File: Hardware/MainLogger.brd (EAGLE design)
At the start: 90 x 70 mm, 163 parts, among them J2 GEMS_POWER_PLUGINPUT, J3 CONN_TALON_LOGGER, J4 U.FL, J5 CONN_TALON_LOGGER, J6 CONN_TALON_LOGGER, J8 CONN_TALON_LOGGER, Q1 DMG3404, Q2 MOSFET_PCH-DMP3036SFG, Q3 MOSFET_PCH-DMP3036SFG, Q4 DMG3404, Q5 NX2301P, U1 MMC5633, U10 MXC6655, U11 FXMAR2102UMLP, U12 MCP79412SOIC, U13 SN74LVC1G17DCK, U14 TPL5010DDC, U15 MIC842L, U16 TPL5010DDC, U17 TPL5010DDC, U18 HALL_EFFECT_SI7201, U19 LP59073.3VYKE, U2 PAC1934QFN, U21 MIC22602, U3 LTC4412S6, U4 BQ25616, U5 TPS78218DBV, U6 MAX-M8W, U7 B_SERIES_M.2EKEY_3042, U8 TCR2LE31ESV, U9 TPS61282D

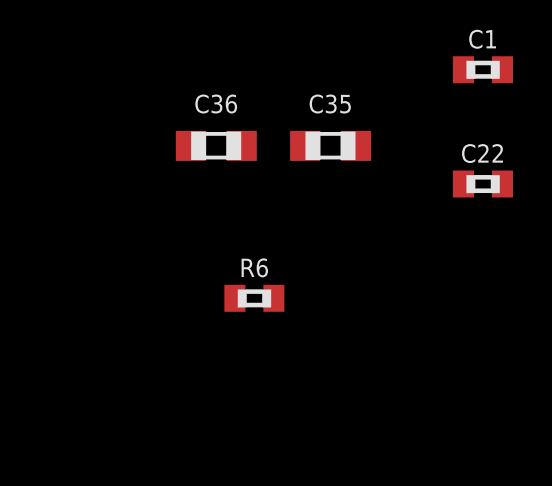
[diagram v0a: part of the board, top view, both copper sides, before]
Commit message: Added VELM3328
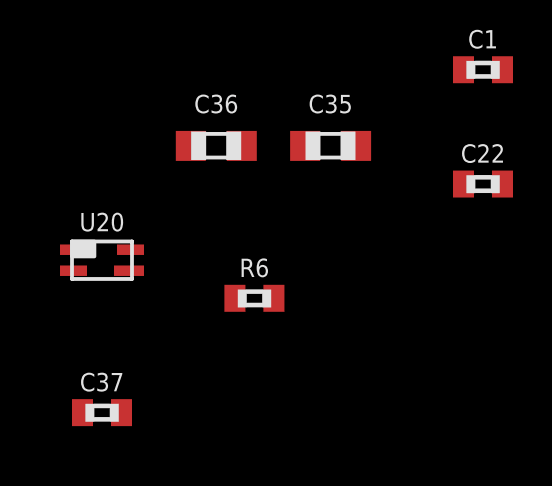
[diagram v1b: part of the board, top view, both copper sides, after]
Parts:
- added C37: (no value), bschulz_passives:C0402
- added U20: VEML3328, bschulz:VEML6075
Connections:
- net 3V3_AUX: now also C37.1, U20.4
- net GND: now also C37.2, U20.1
- net SCL_OB: now also U20.3
- net SDA_OB: now also U20.2
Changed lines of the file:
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@@
 <attribute name="VALUE_PART" value="10k" x="-128.27" y="-170.18" size="1.778" layer="27" font="vector" ratio="15" display="off"/>
+</element>
+<element name="U20" library="bschulz" package="VEML6075" value="VEML3328" x="-133.35" y="-168.91" smashed="yes">
+<attribute name="DIGIKEY" value="751-VEML3328CT-ND" x="-133.35" y="-168.91" size="1.778" layer="27" font="vector" ratio="15" display="off"/>
+<attribute name="DISP" value="VEML3328" x="-133.35" y="-168.91" size="1.778" layer="27" font="vector" ratio="15" display="off"/>
+<attribute name="MF" value="Vishay" x="-133.35" y="-168.91" size="1.778" layer="27" font="vector" ratio="15" display="off"/>
+<attribute name="MPN" value="VEML3328" x="-133.35" y="-168.91" size="1.778" layer="27" font="vector" ratio="15" display="off"/>
+<attribute name="NAME" x="-133.35" y="-167.64" size="0.6096" layer="25" font="vector" ratio="15" align="center"/>
+<attribute name="VALUE" x="-133.223" y="-170.18" size="0.6096" layer="27" font="vector" ratio="15" align="center"/>
+</element>
+<element name="C37" library="bschulz_passives" package="C0402" value="" x="-133.35" y="-173.99" smashed="yes">
+<attribute name="DIGIKEY" value="490-4759-1-ND" x="-133.35" y="-173.99" size="1.778" layer="27" font="vector" ratio="15" display="off"/>
+<attribute name="MF" value="Murata" x="-133.35" y="-173.99" size="1.778" layer="27" font="vector" ratio="15" display="off"/>
+<attribute name="MPN" value="GCM155R71C104KA55D" x="-133.35" y="-173.99" size="1.778" layer="27" font="vector" ratio="15" display="off"/>
+<attribute name="NAME" x="-133.35" y="-172.974" size="0.6096" layer="25" font="vector" ratio="15" align="center"/>
+<attribute name="VALUE" x="-133.35" y="-175.006" size="0.6096" layer="27" font="vector" ratio="15" align="center"/>
 </element>
 </elements>
@@
 <contactref element="C35" pad="2"/>
 <contactref element="C36" pad="2"/>
+<contactref element="U20" pad="1"/>
+<contactref element="C37" pad="2"/>
 <wire x1="-84.24" y1="-86.36" x2="-88.05" y2="-86.36" width="0" layer="19" extent="1-1"/>
 <wire x1="-76.82" y1="-86.36" x2="-84.24" y2="-86.36" width="0" layer="19" extent="1-1"/>
@@
 <wire x1="-124.88" y1="-165.1" x2="-120" y2="-166.37" width="0" layer="19" extent="1-1"/>
 <wire x1="-128.69" y1="-165.1" x2="-124.88" y2="-165.1" width="0" layer="19" extent="1-1"/>
+<wire x1="-134.3" y1="-168.56" x2="-128.69" y2="-165.1" width="0" layer="19" extent="1-1"/>
+<wire x1="-132.7" y1="-173.99" x2="-134.3" y2="-168.56" width="0" layer="19" extent="1-1"/>
 </signal>
 <signal name="D+">
@@
 <contactref element="U1" pad="B1"/>
 <contactref element="C36" pad="1"/>
+<contactref element="U20" pad="4"/>
+<contactref element="C37" pad="1"/>
 <wire x1="75.692" y1="13.574" x2="76.835" y2="13.574" width="0" layer="19" extent="1-1"/>
 <wire x1="74.591" y1="10.287" x2="75.692" y2="13.574" width="0" layer="19" extent="1-1"/>
@@
 <wire x1="-120.85" y1="-151.33" x2="64.008" y2="14.59" width="0" layer="19" extent="1-1"/>
 <wire x1="-130.39" y1="-165.1" x2="-120.85" y2="-151.33" width="0" layer="19" extent="1-1"/>
+<wire x1="-132.4" y1="-168.56" x2="-130.39" y2="-165.1" width="0" layer="19" extent="1-1"/>
+<wire x1="-134" y1="-173.99" x2="-132.4" y2="-168.56" width="0" layer="19" extent="1-1"/>
 </signal>
 <signal name="N$4">
@@
 <contactref element="U10" pad="2"/>
 <contactref element="U11" pad="7"/>
+<contactref element="U20" pad="2"/>
 <wire x1="-120.45" y1="-151.33" x2="-20.955" y2="-35.3" width="0" layer="19" extent="1-1"/>
 <wire x1="-120.9" y1="-155.715" x2="-120.45" y2="-151.33" width="0" layer="19" extent="1-1"/>
 <wire x1="-120.65" y1="-158.275" x2="-120.9" y2="-155.715" width="0" layer="19" extent="1-1"/>
+<wire x1="-134.3" y1="-169.26" x2="-120.65" y2="-158.275" width="0" layer="19" extent="1-1"/>
 </signal>
 <signal name="N$14">
@@
 <contactref element="U10" pad="12"/>
 <contactref element="U11" pad="6"/>
+<contactref element="U20" pad="3"/>
+<wire x1="-120.25" y1="-158.275" x2="-132.45" y2="-169.26" width="0" layer="19" extent="1-1"/>
 <wire x1="-121.45" y1="-155.19" x2="-120.25" y2="-158.275" width="0" layer="19" extent="1-1"/>
 <wire x1="-120.45" y1="-150.93" x2="-121.45" y2="-155.19" width="0" layer="19" extent="1-1"/>

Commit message: Continued layout and schematic updates
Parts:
- removed C12, TALON_INTERFACE1:C21: 1uF, bschulz_passives:C0603
- removed C22, C30, C31, TALON_INTERFACE1:C18, TALON_INTERFACE1:C19: 0.1uF, bschulz_passives:C0402
- removed C29: 10uF, bschulz_passives:C0805
- removed D7: LEDRED0603, bschulz:LED_0603
- removed D8: LEDGREEN0603, bschulz:LED_0603
- removed FB6: (no value), bschulz:R0402
- removed J3, J5, J6, J8, TALON_INTERFACE1:J1: CONN_TALON_LOGGER, GEMS_Plugs:1X06_MICROLOCKPLUS_RT
- removed J7: (no value), bschulz:JST-2-SMD
- removed R2, R39, R4, R40, R41, R49: 10k, bschulz_passives:R0402
- removed R22, TALON_INTERFACE1:R35, TALON_INTERFACE1:R36: 100k, bschulz_passives:R0402
- removed R35: 1k, bschulz_passives:R0402
- removed R36: 1k, bschulz_passives:R0603
- removed R42, R43: 4.7k, bschulz_passives:R0603
- removed S1: SP3TCS-4-13NA, bschulz:CS-4-13NA
- removed TALON_INTERFACE1:C20: 2.2uF, bschulz_passives:C0603
- removed TALON_INTERFACE1:C22: 100uF, bschulz_passives:C1411_TANT
- removed TALON_INTERFACE1:U10: FXMAR2102UMLP, bschulz:UQFN-8_1.4X1.2
- removed TALON_INTERFACE1:U11: AP2411, bschulz:MSOP_8EP
- removed TALON_INTERFACE1:U9: FSA2258, bschulz:MICROPAK_10
- added C38, C41, C42, C43, C54, TALON1:C18, TALON1:C19, TALON2:C18, TALON2:C19, TALON3:C18, TALON3:C19, TALON4:C18, TALON4:C19: 0.1uF, bschulz_passives:C0402
- added C39, TALON1:C21, TALON2:C21, TALON3:C21, TALON4:C21: 1uF, bschulz_passives:C0603
- added C40: 0.1uF, bschulz_passives:C0603
- added D1: CLVBA-FKA, bschulz:CLVBA-FKA
- added D10, D12, D13, D14, D15, D16, D17: LED0603, bschulz:LED_0603
- added FB3: (no value), bschulz:R0402
- added H1, H2, H3, H4: (no value), bschulz:4_40
- added J9: (no value), bschulz:JST-2-SMD
- added R10, R52: 10k, bschulz_passives:R0402
- added R51, R71, R72, R73, R74, R75, R76: 220R, bschulz_passives:R0603
- added R54: 100k, bschulz_passives:R0603
- added R60: 0R, bschulz_passives:R0402
- added R63, R64, R65: 2m, bschulz_passives:R0805
- added R66: 10m, bschulz_passives:R0805
- added R67, R68, R69, R70: (no value), bschulz_passives:R0603
- added R7, R8, R9: 4.7k, bschulz_passives:R0603
- added S3, S4: BUTTON4.2X3.2, bschulz:SWITCH_4.2X3.2
- added SD2: MICROSDMOLEX_503182, bschulz:MICROSD_MOLEX_5031821852
- added TALON1:C20, TALON2:C20, TALON3:C20, TALON4:C20: 2.2uF, bschulz_passives:C0603
- added TALON1:C22, TALON2:C22, TALON3:C22, TALON4:C22: 100uF, bschulz_passives:C1411_TANT
- added TALON1:J1, TALON2:J1, TALON3:J1, TALON4:J1: CONN_TALON_LOGGER, GEMS_Plugs:1X06_MICROLOCKPLUS_RT
- added TALON1:R36, TALON2:R36, TALON3:R36, TALON4:R36: 100k, bschulz_passives:R0402
- added TALON1:U1, TALON2:U1, TALON3:U1, TALON4:U1: SN74AUP1G08DCK, bschulz:DCK_R-PDSO-G5
- added TALON1:U10, TALON2:U10, TALON3:U10, TALON4:U10: FXMAR2102UMLP, bschulz:UQFN-8_1.4X1.2
- added TALON1:U11, TALON2:U11, TALON3:U11, TALON4:U11: AP2411, bschulz:MSOP_8EP
- added TALON1:U9, TALON2:U9, TALON3:U9, TALON4:U9: FSA2258, bschulz:MICROPAK_10
- added U23: MB85RC, bschulz:SO08
- added U24: SN74AUP3G34DCU, bschulz:DCU_(R-PDSO-G8)
- added U25: SIP32431TDFN, bschulz:TDFN_4
- added U26: PAC1934QFN, bschulz:QFN16
- added U27: MCP23018QFN, bschulz:QFN24
- added U28: PCA9634QFN, bschulz:QFN20_5X5
- C11: value 1uF -> 0.1uF; device bschulz_passives:C0603 -> bschulz_passives:C0402
- C23, C24: value 6pF -> 9pF
- C37: value (none) -> 0.1uF
- D5: value (none) -> LED0603; device bschulz:SOT23-3 -> bschulz:LED_0603
- R1, R23, R3: value 100k -> 1M
- R20: value 0R -> 100k; device bschulz_passives:R0402 -> bschulz_passives:R0603
- R32: value 10k -> 100k
- R33: value 10k -> 220R; device bschulz_passives:R0402 -> bschulz_passives:R0603
- U14: value TPL5010DDC -> FXMAR2102UMLP; device bschulz:DDC_R-PDSO-G6 -> bschulz:UQFN-8_1.4X1.2
- U15: value MIC842L -> SN74AUP1G08DCK
- U5: value TPS78218DBV -> MCP23018QFN; device bschulz:SOT23-5 -> bschulz:QFN24
- XTAL1: value CRYSTAL3.2X1.5 -> CRYSTAL32.768KHZ_9PF3.2X1.5
- moved C37 272.4 mm to (49.5, 27.9), turned to 270 degrees
- moved R6 270.8 mm to (50.0, 33.7), turned to 180 degrees
- moved U20 269.6 mm to (50.8, 27.9), turned to 90 degrees
- moved C36 263.8 mm to (46.1, 31.8), turned to 90 degrees
- moved C35 263.4 mm to (49.5, 31.5), turned to 270 degrees
- moved U10 254.1 mm to (51.7, 31.8), turned to 90 degrees
- moved C1 252.9 mm to (45.7, 27.9), turned to 270 degrees
- moved U11 251.0 mm to (47.1, 27.9)
- moved U1 248.5 mm to (47.6, 31.8)
- moved R50 239.0 mm to (38.1, 33.4), turned to 180 degrees
- moved C32 209.5 mm to (66.4, 65.9)
- moved R48 202.0 mm to (65.8, 61.1), turned to 180 degrees
- moved R47 201.1 mm to (63.4, 65.9)
- moved C28 195.7 mm to (60.2, 65.0), turned to 90 degrees
- moved C27 194.7 mm to (84.8, 58.3)
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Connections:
- removed net !PG: D4.CATHODE, R29.1, R35.2, U4.7
- removed net 3V3: C13.1, C15.1, C25.1, C30.1, C31.1, R32.2, R33.2, R38.2, R39.2, U12.8, U14.1, U15.5, U6.7, U6.8, U7.10, U7.12
- removed net 3V3_EXT_FAULT: D7.CATHODE
- removed net AGND: U7.39, U7.49
- removed net ALERT: R3.1, U2.1
- removed net BYPASS: U9.C1
- removed net EN: U9.A1
- removed net N$11: R22.1, S1.3
- removed net N$14: R40.2, U14.3
- removed net N$16: C29.1, R41.2, U15.1
- removed net N$19: R39.1, R41.1, U14.6
- removed net N$26: R42.2, R43.2, U15.4
- removed net N$27: D7.ANODE, R42.1
- removed net N$28: D8.ANODE, R43.1
- removed net N$31: R35.1
- removed net N$34: R36.1
- removed net N$8: R21.1, S1.2
- removed net N$9: R20.1, S1.1
- removed net PG: R55.1, U21.5, U9.A2
- removed net SEL: U9.B1
- removed net ST: Q4.3, R23.1
- removed net STAT: D3.CATHODE, R26.1, R36.2, U4.5
- removed net TALON_INTERFACE1:!FAULT: TALON_INTERFACE1:R36.1, TALON_INTERFACE1:U11.5
- removed net TALON_INTERFACE1:3V3: TALON_INTERFACE1:C18.1, TALON_INTERFACE1:C20.1, TALON_INTERFACE1:R36.2, TALON_INTERFACE1:U10.1, TALON_INTERFACE1:U11.2, TALON_INTERFACE1:U11.3
- removed net TALON_INTERFACE1:3V3_TALON: TALON_INTERFACE1:C19.1, TALON_INTERFACE1:C21.1, TALON_INTERFACE1:C22.ANODE, TALON_INTERFACE1:J1.2, TALON_INTERFACE1:U10.8, TALON_INTERFACE1:U11.6, TALON_INTERFACE1:U11.7, TALON_INTERFACE1:U9.10
- removed net TALON_INTERFACE1:EN: TALON_INTERFACE1:U11.4
- removed net TALON_INTERFACE1:GND: TALON_INTERFACE1:C18.2, TALON_INTERFACE1:C19.2, TALON_INTERFACE1:C20.2, TALON_INTERFACE1:C21.2, TALON_INTERFACE1:C22.CATHODE, TALON_INTERFACE1:J1.1, TALON_INTERFACE1:R35.1, TALON_INTERFACE1:U10.4, TALON_INTERFACE1:U11.1, TALON_INTERFACE1:U11.EP, TALON_INTERFACE1:U9.5
- removed net TALON_INTERFACE1:GPIOA: TALON_INTERFACE1:U9.2
- removed net TALON_INTERFACE1:GPIOB: TALON_INTERFACE1:U9.4
- removed net TALON_INTERFACE1:I2C_EN: TALON_INTERFACE1:R35.2, TALON_INTERFACE1:U10.5
- removed net TALON_INTERFACE1:RX: TALON_INTERFACE1:U9.3
- removed net TALON_INTERFACE1:RX_TALON: TALON_INTERFACE1:J1.6, TALON_INTERFACE1:U9.6
- removed net TALON_INTERFACE1:SCL: TALON_INTERFACE1:U10.3
- removed net TALON_INTERFACE1:SCL_EXT: TALON_INTERFACE1:J1.4, TALON_INTERFACE1:U10.6
- removed net TALON_INTERFACE1:SDA: TALON_INTERFACE1:U10.2
- removed net TALON_INTERFACE1:SDA_EXT: TALON_INTERFACE1:J1.3, TALON_INTERFACE1:U10.7
- removed net TALON_INTERFACE1:SEL: TALON_INTERFACE1:U9.7, TALON_INTERFACE1:U9.8
- removed net TALON_INTERFACE1:TX: TALON_INTERFACE1:U9.1
- removed net TALON_INTERFACE1:TX_TALON: TALON_INTERFACE1:J1.5, TALON_INTERFACE1:U9.9
- removed net TIMEPULSE: FB6.2, U6.4
- removed net TIMEPULSE_EXT: FB6.1
- removed net UB_VBUS: U7.74
- removed net VBAT: C20.1, C21.+, L2.P$1, U9.A3, U9.A4
- removed net VCC: U7.2, U7.4, U7.6, U7.8
- removed net VLOGIC: C2.1, C3.1, D5.3, R1.2, R23.2, R3.2, U2.15, U2.2
- removed net VLOGIC_BUS: D5.2, J2.5, R2.2, R4.2
- removed net VOUT: C18.1, C19.1, U9.B3, U9.B4
- removed net V_BACKUP: C14.1, U6.6
- new net !CHG_PG: D4.CATHODE, R29.1, U27.18, U4.7
- new net !TALON1_FAULT: TALON1:R36.1, TALON1:U11.5, TALON2:R36.1, TALON2:U11.5, TALON3:R36.1, TALON3:U11.5, TALON4:R36.1, TALON4:U11.5, U5.4
- new net !TALON2_FAULT: U5.5
- new net !TALON3_FAULT: U5.6
- new net !TALON4_FAULT: U5.7
- new net 3V3_AUX_PG: R55.1, U21.5, U27.15
- new net 3V3_BULK: R65.1, TALON1:C18.1, TALON1:C20.1, TALON1:R36.2, TALON1:U1.5, TALON1:U10.1, TALON1:U11.2, TALON1:U11.3, TALON2:C18.1, TALON2:C20.1, TALON2:R36.2, TALON2:U1.5, TALON2:U10.1, TALON2:U11.2, TALON2:U11.3, TALON3:C18.1, TALON3:C20.1, TALON3:R36.2, TALON3:U1.5, TALON3:U10.1, TALON3:U11.2, TALON3:U11.3, TALON4:C18.1, TALON4:C20.1, TALON4:R36.2, TALON4:U1.5, TALON4:U10.1, TALON4:U11.2, TALON4:U11.3, U26.9
- new net 3V3_BULK+: C44.1, C46.ANODE, L3.P$2, R55.2, R56.2, R64.2, R65.2, U26.10, U26.8
- new net 3V3_CORE+: C34.1, R66.1, U19.A2, U26.13
- new net 3V3_SD: C40.1, R20.2, U24.8, U25.1
- new net 3V3_SD_EN: R54.2, U25.4, U27.4
- new net CHG_SOURCE: Q4.3, R23.1, U27.20
- new net CHG_STAT: D3.CATHODE, R26.1, U27.19, U4.5
- new net CSA_ALERT: R3.1, U2.1, U26.1, U27.17
- new net I2C_EN_GLOBAL: U15.1
- new net I2C_EXT_EN: U15.2, U27.2
- new net I2C_EXT_EN_OUT: U14.5, U15.4
- new net I2C_GLOBAL_EN: TALON1:U1.1, TALON2:U1.1, TALON3:U1.1, TALON4:U1.1, U7.64
- new net LED_BLUE: R7.2, U7.65
- new net LED_EN: R32.1, U27.5, U28.13, U7.47
- new net LED_GREEN: R8.2, U7.63
- new net LED_RED: R9.2, U7.61
- new net MISO: SD2.7, U7.50
- new net MOSI: U24.1, U7.52
- new net MOSI_BUF: SD2.3, U24.7
- new net N$15: R50.1, U27.1
- new net N$21: D1.3, R7.1
- new net N$22: D1.4, R8.1
- new net N$23: D1.1, R9.1
- new net N$24: FB3.1, U6.9
- new net N$36: D5.CATHODE, U28.4
- new net N$37: D10.CATHODE, U28.5
- new net N$38: R67.2, R68.1, U27.11
- new net N$39: D12.CATHODE, U28.6
- new net N$40: D13.CATHODE, U28.7
- new net N$41: D14.CATHODE, U28.9
- new net N$42: D15.CATHODE, U28.10
- new net N$43: D16.CATHODE, U28.11
- new net N$44: D17.CATHODE, U28.12
- new net N$45: D5.ANODE, R33.1
- new net N$46: D10.ANODE, R51.1
- new net N$47: D12.ANODE, R71.1
- new net N$48: D13.ANODE, R72.1
- new net N$49: D14.ANODE, R73.1
- new net N$50: D15.ANODE, R74.1
- new net N$51: D16.ANODE, R75.1
- new net N$52: D17.ANODE, R76.1
- new net OB_INT: U27.14, U7.43
- new net SCK: U24.3, U7.54
- new net SCK_BUF: SD2.5, U24.5
- new net SCL_GPS: FB2.2, U6.17
- new net SDA_GPS: FB1.2, U6.16
- new net SD_CD: R20.1, SD2.SW2, U27.22
- new net SD_CS: U24.6, U7.48
- new net SD_CS_BUF: SD2.2, U24.2
- new net TALON1:3V3_TALON: TALON1:C19.1, TALON1:C21.1, TALON1:C22.ANODE, TALON1:J1.2, TALON1:U10.8, TALON1:U11.6, TALON1:U11.7, TALON1:U9.10
- new net TALON1:GPIOA: TALON1:U9.2
- new net TALON1:GPIOB: TALON1:U9.4
- new net TALON1:I2C_EN_LOCAL: TALON1:U1.4, TALON1:U10.5
- new net TALON1:RX_TALON: TALON1:J1.6, TALON1:U9.6
- new net TALON1:SCL_EXT: TALON1:J1.4, TALON1:U10.6
- new net TALON1:SDA_EXT: TALON1:J1.3, TALON1:U10.7
- new net TALON1:TX_TALON: TALON1:J1.5, TALON1:U9.9
- new net TALON1_EN: TALON1:U11.4, TALON2:U11.4, TALON3:U11.4, TALON4:U11.4, U5.19
- new net TALON1_GPIOA: U7.23
- new net TALON1_GPIOB: U7.66
- new net TALON1_I2C_EN: TALON1:U1.2, TALON2:U1.2, TALON3:U1.2, TALON4:U1.2, U5.24
- new net TALON1_SEL: TALON1:U9.7, TALON1:U9.8, TALON2:U9.7, TALON2:U9.8, TALON3:U9.7, TALON3:U9.8, TALON4:U9.7, TALON4:U9.8, U5.15
- new net TALON2:3V3_TALON: TALON2:C19.1, TALON2:C21.1, TALON2:C22.ANODE, TALON2:J1.2, TALON2:U10.8, TALON2:U11.6, TALON2:U11.7, TALON2:U9.10
- new net TALON2:GPIOA: TALON2:U9.2
- new net TALON2:GPIOB: TALON2:U9.4
- new net TALON2:I2C_EN_LOCAL: TALON2:U1.4, TALON2:U10.5
- new net TALON2:RX_TALON: TALON2:J1.6, TALON2:U9.6
- new net TALON2:SCL_EXT: TALON2:J1.4, TALON2:U10.6
- new net TALON2:SDA_EXT: TALON2:J1.3, TALON2:U10.7
- new net TALON2:TX_TALON: TALON2:J1.5, TALON2:U9.9
- new net TALON2_EN: U5.20
- new net TALON2_GPIOA: U7.33
- new net TALON2_GPIOB: U7.68
- new net TALON2_I2C_EN: U5.1
- new net TALON2_SEL: U5.16
- new net TALON3:3V3_TALON: TALON3:C19.1, TALON3:C21.1, TALON3:C22.ANODE, TALON3:J1.2, TALON3:U10.8, TALON3:U11.6, TALON3:U11.7, TALON3:U9.10
- new net TALON3:GPIOA: TALON3:U9.2
- new net TALON3:GPIOB: TALON3:U9.4
- new net TALON3:I2C_EN_LOCAL: TALON3:U1.4, TALON3:U10.5
- new net TALON3:RX_TALON: TALON3:J1.6, TALON3:U9.6
- new net TALON3:SCL_EXT: TALON3:J1.4, TALON3:U10.6
- new net TALON3:SDA_EXT: TALON3:J1.3, TALON3:U10.7
- new net TALON3:TX_TALON: TALON3:J1.5, TALON3:U9.9
- new net TALON3_EN: U5.21
- new net TALON3_GPIOA: U7.35
- new net TALON3_GPIOB: U7.70
- new net TALON3_I2C_EN: U5.2
- new net TALON3_SEL: U5.17
- new net TALON4:3V3_TALON: TALON4:C19.1, TALON4:C21.1, TALON4:C22.ANODE, TALON4:J1.2, TALON4:U10.8, TALON4:U11.6, TALON4:U11.7, TALON4:U9.10
- new net TALON4:GPIOA: TALON4:U9.2
- new net TALON4:GPIOB: TALON4:U9.4
- new net TALON4:I2C_EN_LOCAL: TALON4:U1.4, TALON4:U10.5
- new net TALON4:RX_TALON: TALON4:J1.6, TALON4:U9.6
- new net TALON4:SCL_EXT: TALON4:J1.4, TALON4:U10.6
- new net TALON4:SDA_EXT: TALON4:J1.3, TALON4:U10.7
- new net TALON4:TX_TALON: TALON4:J1.5, TALON4:U9.9
- new net TALON4_EN: U5.22
- new net TALON4_GPIOA: U7.37
- new net TALON4_GPIOB: U7.72
- new net TALON4_I2C_EN: U5.3
- new net TALON4_SEL: U5.18
- new net TALON_INT: U5.14, U7.41
- new net VBULK: C33.1, C48.1, C49.1, C50.1, C53.1, R63.1, U19.A1, U19.B1, U21.1, U21.13, U21.17, U21.18, U21.6, U26.12
- new net VBULK+: C18.1, C19.1, R63.2, U26.11, U9.B3, U9.B4
- new net VBULK_PG: U27.16, U9.A2
- new net VDD: SD2.4
- net !CE: now also U27.3
- net !MODE: now also R10.1, S4.1, S4.2
- net !RESET: now also FB3.2, R52.1, S3.1, S3.2, U27.12, U5.12; no longer R49.1
- net 3V3_AUX: now also C13.1, C15.1, C39.1, J2.5, R64.1, U25.3, U26.7, U6.7, U6.8; no longer C44.1, C46.ANODE, L3.P$2, R55.2, R56.2
- net 3V3_AUX_EN: now also U27.7
- net 3V3_CORE: now also C11.1, C2.1, C25.1, C3.1, C38.1, C41.1, C42.1, C43.1, C54.1, D1.2, R1.2, R10.2, R23.2, R3.2, R32.2, R33.2, R38.2, R51.2, R52.2, R66.2, R68.2, R70.2, R71.2, R72.2, R73.2, R74.2, R75.2, R76.2, U12.8, U14.1, U14.8, U15.5, U2.15, U2.2, U23.1, U23.2, U23.3, U23.8, U26.14, U26.15, U26.2, U27.8, U28.18, U5.8, U7.10, U7.12; no longer C22.1, C34.1, R49.2, U19.A2
- net ACCEL_INT: now also U27.21
- net BCKP_GPS: now also C14.1, U6.6
- net CSA_EN: now also U26.16, U27.6
- net D+: now also U7.11, U7.44
- net D-: now also U7.13, U7.46
- net GND: now also C38.2, C39.2, C40.2, C41.2, C42.2, C43.2, C54.2, R54.1, R60.1, R67.1, R69.1, S3.3, S3.4, S4.3, S4.4, SD2.6, SD2.BODY@1, SD2.BODY@2, SD2.BODY@3, SD2.BODY@4, SD2.BODY@5, SD2.SW1, TALON1:C18.2, TALON1:C19.2, TALON1:C20.2, TALON1:C21.2, TALON1:C22.CATHODE, TALON1:J1.1, TALON1:U1.3, TALON1:U10.4, TALON1:U11.1, TALON1:U11.EP, TALON1:U9.5, TALON2:C18.2, TALON2:C19.2, TALON2:C20.2, TALON2:C21.2, TALON2:C22.CATHODE, TALON2:J1.1, TALON2:U1.3, TALON2:U10.4, TALON2:U11.1, TALON2:U11.EP, TALON2:U9.5, TALON3:C18.2, TALON3:C19.2, TALON3:C20.2, TALON3:C21.2, TALON3:C22.CATHODE, TALON3:J1.1, TALON3:U1.3, TALON3:U10.4, TALON3:U11.1, TALON3:U11.EP, TALON3:U9.5, TALON4:C18.2, TALON4:C19.2, TALON4:C20.2, TALON4:C21.2, TALON4:C22.CATHODE, TALON4:J1.1, TALON4:U1.3, TALON4:U10.4, TALON4:U11.1, TALON4:U11.EP, TALON4:U9.5, U15.3, U23.4, U23.7, U24.4, U25.2, U25.EP, U26.3, U26.EP, U27.23, U27.EP, U28.8, U28.EP, U5.23, U5.EP, U7.39, U7.49; no longer C12.2, C22.2, C29.2, C30.2, C31.2, D8.CATHODE, R20.2, R22.2, R40.1, U14.2, U15.2, U5.2, U5.4
- net GPS_INT: now also U27.24
- net I2C_OB_EN: now also U7.45
- net N$17: now also R60.2, U26.6; no longer C12.1, D5.1, U5.5
- net N$35: now also R69.2, R70.1, U5.11; no longer R50.1
- net RTC_INT: now also U7.62
- net RX: now also TALON1:U9.3, TALON2:U9.3, TALON3:U9.3, TALON4:U9.3, U7.38; no longer U6.3
- net SCL: now also TALON1:U10.3, TALON2:U10.3, TALON3:U10.3, TALON4:U10.3, U14.3, U7.20; no longer FB2.2, J2.6, R2.1, U12.6, U2.4, U6.17
- net SCL_EXT: now also J2.6, U14.6; no longer FB2.1, R33.1
- net SCL_OB: now also FB2.1, U12.6, U2.4, U23.6, U26.4, U27.9, U28.16, U5.9
- net SDA: now also TALON1:U10.2, TALON2:U10.2, TALON3:U10.2, TALON4:U10.2, U14.2, U7.22; no longer FB1.2, J2.4, R4.1, U2.5, U6.16
- net SDA_EXT: now also J2.4, U14.7; no longer FB1.1, R32.1
- net SDA_OB: now also FB1.1, U2.5, U23.5, U26.5, U27.10, U28.17, U5.10
- net SYS: now also C20.1, C21.+, L2.P$1, U7.2, U7.4, U7.6, U7.8, U9.A1, U9.A3, U9.A4, U9.B1, U9.C1; no longer C11.1, C33.1, C48.1, C49.1, C50.1, C53.1, U19.A1, U19.B1, U21.1, U21.13, U21.17, U21.18, U21.6, U5.1, U5.3
- net TEST: now also U7.40
- net TX: now also TALON1:U9.1, TALON2:U9.1, TALON3:U9.1, TALON4:U9.1, U7.36; no longer U6.2
- net VBUS: no longer U7.16
- net VSET: now also R21.1; no longer S1.C
- net VUSB: now also U7.16, U7.74
- net WDT_DONE: now also U7.42
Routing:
- net GND: track 137.3 -> 469.9 mm, vias 20 -> 36
- net 3V3_CORE: track 0.69 -> 217.3 mm
- net SDA_OB: track 0.00 -> 186.5 mm, vias 0 -> 8
- net SCL_OB: track 0.00 -> 183.8 mm, vias 0 -> 10
- net BAT_CHG: track 24.5 -> 113.6 mm, vias 2 -> 6
- net CSA_ALERT: track 0.00 -> 78.7 mm, vias 0 -> 4
- net VLOGIC: track 76.4 -> 0.00 mm, vias 6 -> 0
- net 3V3_AUX: track 21.2 -> 96.8 mm, vias 0 -> 8
- net SYS: track 38.5 -> 112.4 mm, vias 0 -> 1
- net D+: track 18.6 -> 89.2 mm
- net 3V3_BULK: track 0.00 -> 68.6 mm, vias 0 -> 3
- net D-: track 19.9 -> 85.7 mm
- net ST: track 64.9 -> 0.00 mm, vias 2 -> 0
- net VBULK: track 0.00 -> 63.1 mm, vias 0 -> 14
- net VUSB: track 11.2 -> 73.5 mm
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- added copper zone on layer 1, net 3V3_BULK+
- added copper zone on layer 1, net 3V3_CORE+
- added copper zone on layer 1, net GPS_ANT
- added copper zone on layer 1, net SYS
- added copper zone on layer 16, net SYS
- added copper zone on layer 1, net VBULK
- added copper zone on layer 16, net VBULK
- added copper zone on layer 1, net VBULK+
- removed copper zone on layer 1, net 3V3_AUX
- removed copper zone on layer 1, net 3V3_CORE
- removed copper zone on layer 16, net 3V3_CORE
- removed copper zone on layer 1, net VBAT
- removed copper zone on layer 1, net VOUT
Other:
- board text added: "PUSH HERE"
- board text removed: "AUX"

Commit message: Initial copper layout complete, cleanup and silk required
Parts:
- C40: device bschulz_passives:C0603 -> bschulz_passives:C0402
- R20, R54: device bschulz_passives:R0603 -> bschulz_passives:R0402
- moved TALON3:C19 452.5 mm to (55.2, 10.7), turned to 270 degrees
- moved TALON3:C21 452.0 mm to (58.4, 11.4)
- moved TALON3:R36 451.4 mm to (56.4, 17.1), turned to 90 degrees
- moved TALON3:U11 449.3 mm to (58.4, 14.1), turned to 180 degrees
- moved TALON3:U9 445.1 mm to (52.1, 7.75), turned to 180 degrees
- moved TALON3:C20 444.9 mm to (60.5, 16.8), turned to 180 degrees
- moved TALON3:U10 442.7 mm to (54.6, 7.62), turned to 180 degrees
- moved TALON3:C22 442.3 mm to (58.4, 8.89)
- moved TALON3:C18 441.0 mm to (54.1, 10.7), turned to 270 degrees
- moved TALON3:J1 435.4 mm to (54.6, 5.08), turned to 180 degrees
- moved TALON3:U1 430.7 mm to (52.1, 10.7), turned to 270 degrees
- moved TALON2:C19 427.6 mm to (42.5, 10.7), turned to 270 degrees
- moved TALON2:C21 427.2 mm to (45.7, 11.4)
- moved TALON2:R36 426.5 mm to (43.7, 17.1), turned to 90 degrees
- moved TALON2:U11 424.6 mm to (45.7, 14.1), turned to 180 degrees
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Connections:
- removed net I2C_EN_GLOBAL: U15.1
- removed net TALON1:GPIOA: TALON1:U9.2
- removed net TALON1:GPIOB: TALON1:U9.4
- removed net TALON2:GPIOA: TALON2:U9.2
- removed net TALON2:GPIOB: TALON2:U9.4
- removed net TALON3:GPIOA: TALON3:U9.2
- removed net TALON3:GPIOB: TALON3:U9.4
- removed net TALON4:GPIOA: TALON4:U9.2
- removed net TALON4:GPIOB: TALON4:U9.4
- removed net VDD: SD2.4
- net !TALON1_FAULT: now also U5.17; no longer TALON2:R36.1, TALON2:U11.5, TALON3:R36.1, TALON3:U11.5, TALON4:R36.1, TALON4:U11.5, U5.4
- net !TALON2_FAULT: now also TALON2:R36.1, TALON2:U11.5, U5.21; no longer U5.5
- net !TALON3_FAULT: now also TALON3:R36.1, TALON3:U11.5, U5.2; no longer U5.6
- net !TALON4_FAULT: now also TALON4:R36.1, TALON4:U11.5, U5.6; no longer U5.7
- net 3V3_BULK: no longer TALON1:U10.1, TALON2:U10.1, TALON3:U10.1, TALON4:U10.1
- net 3V3_CORE: now also U28.15, U28.3
- net 3V3_SD: now also SD2.4
- net GND: now also J9.1, U28.1, U28.14, U28.19, U28.2, U28.20
- net I2C_GLOBAL_EN: now also U15.1
- net LED_EN: no longer U7.47
- net SOLAR+: now also J9.2
- net TALON1:3V3_TALON: now also TALON1:U10.1
- net TALON1_EN: now also U5.18; no longer TALON2:U11.4, TALON3:U11.4, TALON4:U11.4, U5.19
- net TALON1_GPIOA: now also TALON1:U9.2, U7.37; no longer U7.23
- net TALON1_GPIOB: now also TALON1:U9.4, U7.72; no longer U7.66
- net TALON1_I2C_EN: now also U5.16; no longer TALON2:U1.2, TALON3:U1.2, TALON4:U1.2, U5.24
- net TALON1_SEL: no longer TALON2:U9.7, TALON2:U9.8, TALON3:U9.7, TALON3:U9.8, TALON4:U9.7, TALON4:U9.8
- net TALON2:3V3_TALON: now also TALON2:U10.1
- net TALON2_EN: now also TALON2:U11.4, U5.22; no longer U5.20
- net TALON2_GPIOA: now also TALON2:U9.2, U7.35; no longer U7.33
- net TALON2_GPIOB: now also TALON2:U9.4, U7.70; no longer U7.68
- net TALON2_I2C_EN: now also TALON2:U1.2, U5.20; no longer U5.1
- net TALON2_SEL: now also TALON2:U9.7, TALON2:U9.8, U5.19; no longer U5.16
- net TALON3:3V3_TALON: now also TALON3:U10.1
- net TALON3_EN: now also TALON3:U11.4, U5.3; no longer U5.21
- net TALON3_GPIOA: now also TALON3:U9.2, U7.33; no longer U7.35
- net TALON3_GPIOB: now also TALON3:U9.4, U7.68; no longer U7.70
- net TALON3_I2C_EN: now also TALON3:U1.2, U5.1; no longer U5.2
- net TALON3_SEL: now also TALON3:U9.7, TALON3:U9.8, U5.24; no longer U5.17
- net TALON4:3V3_TALON: now also TALON4:U10.1
- net TALON4_EN: now also TALON4:U11.4, U5.7; no longer U5.22
- net TALON4_GPIOA: now also TALON4:U9.2, U7.23; no longer U7.37
- net TALON4_GPIOB: now also TALON4:U9.4, U7.66; no longer U7.72
- net TALON4_I2C_EN: now also TALON4:U1.2, U5.5; no longer U5.3
- net TALON4_SEL: now also TALON4:U9.7, TALON4:U9.8, U5.4; no longer U5.18
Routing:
- net GND: track 469.9 -> 796.9 mm, vias 36 -> 53
- net 3V3_CORE: track 217.3 -> 355.6 mm, vias 10 -> 18
- net SDA: track 52.0 -> 152.7 mm, vias 2 -> 8
- net SCL: track 51.4 -> 151.9 mm, vias 2 -> 6
- net 3V3_BULK: track 68.6 -> 156.5 mm, vias 3 -> 11
- net 3V3_AUX: track 96.8 -> 165.6 mm, vias 8 -> 9
- net !RESET: track 57.6 -> 125.0 mm, vias 2 -> 5
- net 3V3_SD_EN: track 0.00 -> 58.5 mm, vias 0 -> 2
- net I2C_GLOBAL_EN: track 51.6 -> 110.0 mm, vias 0 -> 6
- net TX: track 51.0 -> 109.3 mm, vias 0 -> 6
- net RX: track 50.3 -> 108.1 mm, vias 0 -> 6
- net I2C_EXT_EN: track 0.00 -> 52.6 mm, vias 0 -> 4
- net VUSB: track 73.5 -> 118.2 mm, vias 0 -> 3
- net TALON4_EN: track 0.00 -> 43.1 mm
- net TALON4_SEL: track 0.00 -> 41.8 mm, vias 0 -> 2
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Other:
- outline, holes or cut-outs redrawn
